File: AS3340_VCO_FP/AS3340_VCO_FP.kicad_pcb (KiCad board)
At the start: 2 copper layers, 50.3 x 127.3 mm, 5 parts

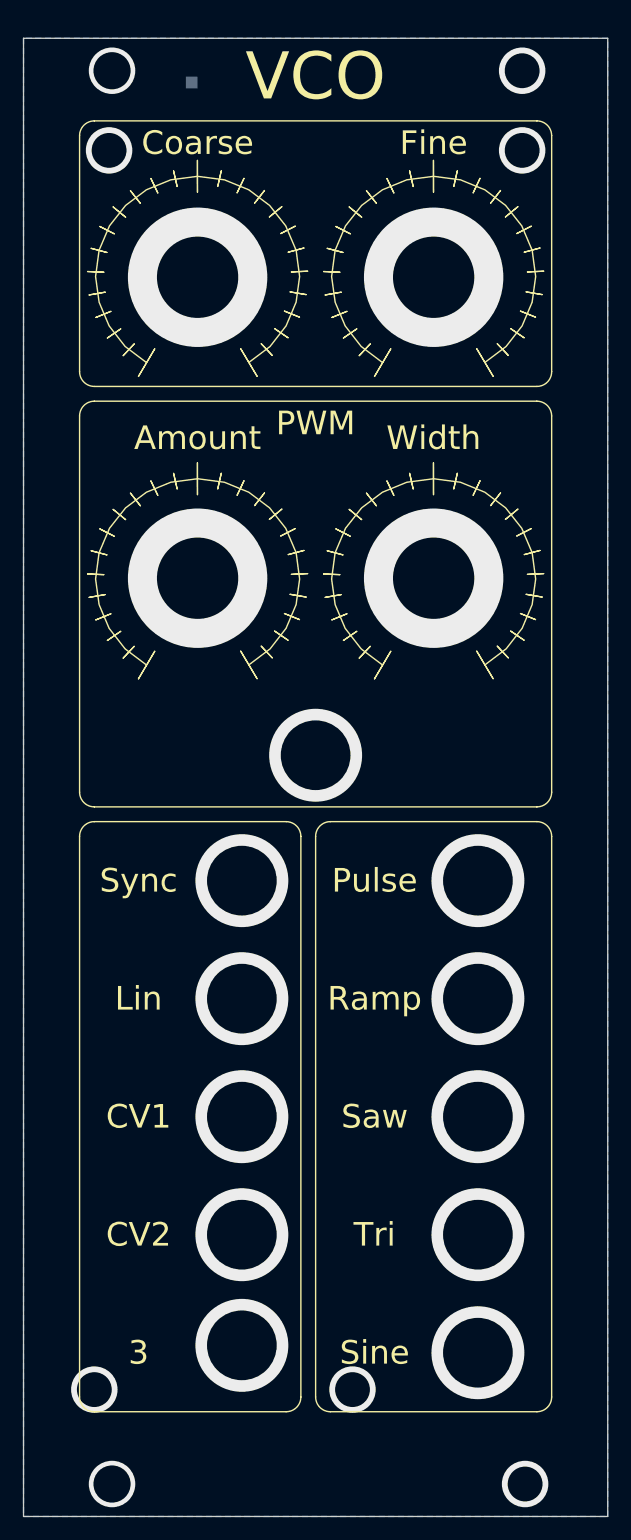
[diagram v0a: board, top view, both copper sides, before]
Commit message: Combine IO and main ADSR boards
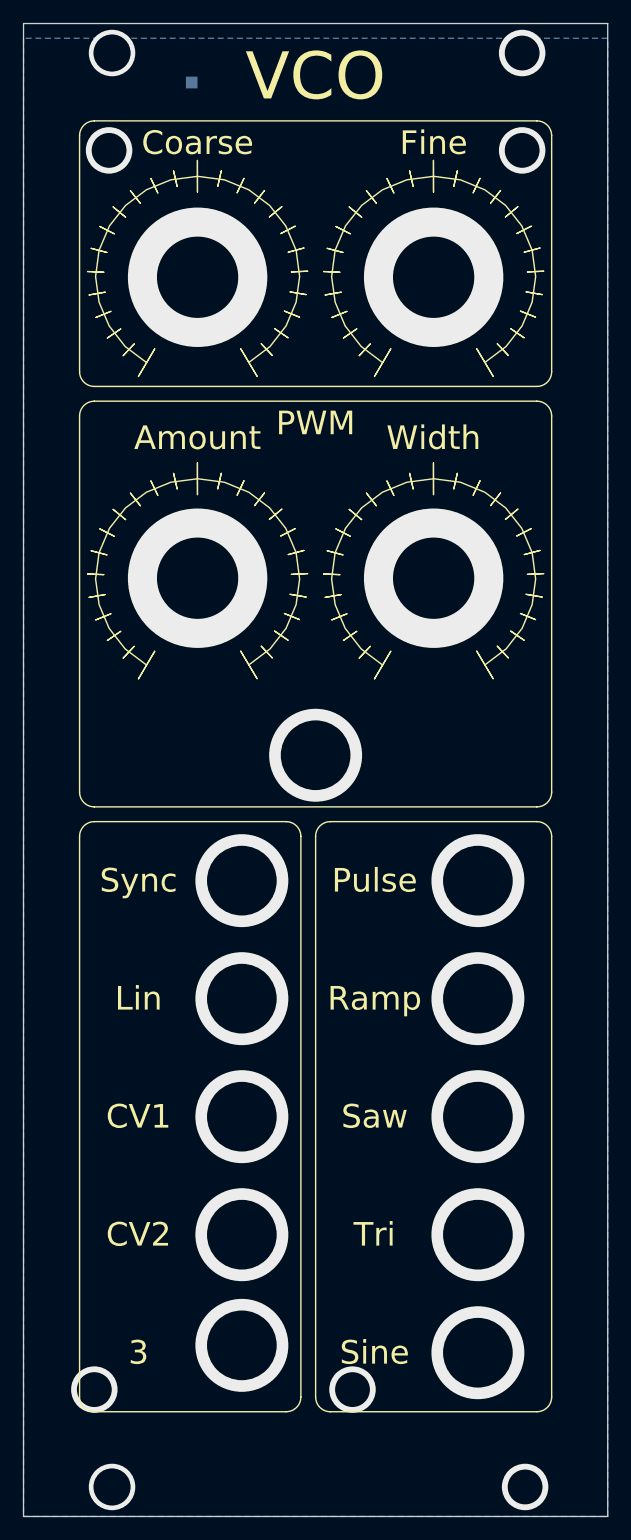
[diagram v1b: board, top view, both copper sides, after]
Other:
- board size 50.3 x 127.3 mm -> 50.3 x 128.5 mm
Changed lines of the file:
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@@
     (effects (font (size 2.032 2.032) (thickness 0.2032)))
   )
-  (gr_line (start 63.754 168.402) (end 63.754 41.148) (layer Edge.Cuts) (width 0.05))
+  (gr_line (start 63.754 168.402) (end 63.754 39.878) (layer Edge.Cuts) (width 0.05))
   (gr_line (start 114.046 168.402) (end 63.754 168.402) (layer Edge.Cuts) (width 0.05))
-  (gr_line (start 114.046 41.148) (end 114.046 168.402) (layer Edge.Cuts) (width 0.05))
-  (gr_line (start 63.754 41.148) (end 114.046 41.148) (layer Edge.Cuts) (width 0.05))
+  (gr_line (start 114.046 39.878) (end 114.046 168.402) (layer Edge.Cuts) (width 0.05))
+  (gr_line (start 63.754 39.878) (end 114.046 39.878) (layer Edge.Cuts) (width 0.05))
   (via (at 69.85 157.48) (size 4) (drill 2.999999) (layers F.Cu B.Cu) (net 1))
   (via (at 92.075 157.48) (size 4) (drill 2.999999) (layers F.Cu B.Cu) (net 1))
@@
   (via (at 78.74 87.63) (size 11.999999) (drill 7.000001) (layers F.Cu B.Cu) (net 1))
   (via (at 78.74 61.722) (size 11.999999) (drill 7.000001) (layers F.Cu B.Cu) (net 1))
-  (via (at 71.374 43.942) (size 4) (drill 3.2004) (layers F.Cu B.Cu) (net 1))
-  (via (at 71.374 165.608) (size 4) (drill 3.2004) (layers F.Cu B.Cu) (net 1))
-  (via (at 106.934 165.608) (size 4) (drill 2.999999) (layers F.Cu B.Cu) (net 1))
-  (via (at 106.68 43.942) (size 4) (drill 2.999999) (layers F.Cu B.Cu) (net 1))
+  (via (at 71.374 42.418) (size 4) (drill 3.2004) (layers F.Cu B.Cu) (net 1))
+  (via (at 71.374 165.862) (size 4) (drill 3.2004) (layers F.Cu B.Cu) (net 1))
+  (via (at 106.934 165.862) (size 4) (drill 2.999999) (layers F.Cu B.Cu) (net 1))
+  (via (at 106.68 42.418) (size 4) (drill 2.999999) (layers F.Cu B.Cu) (net 1))
   (zone (net 1) (net_name GND) (layer B.Cu) (hatch edge 0.508)
     (connect_pads yes (clearance 0.508))
